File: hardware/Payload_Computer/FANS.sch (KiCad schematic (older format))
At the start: 0 parts

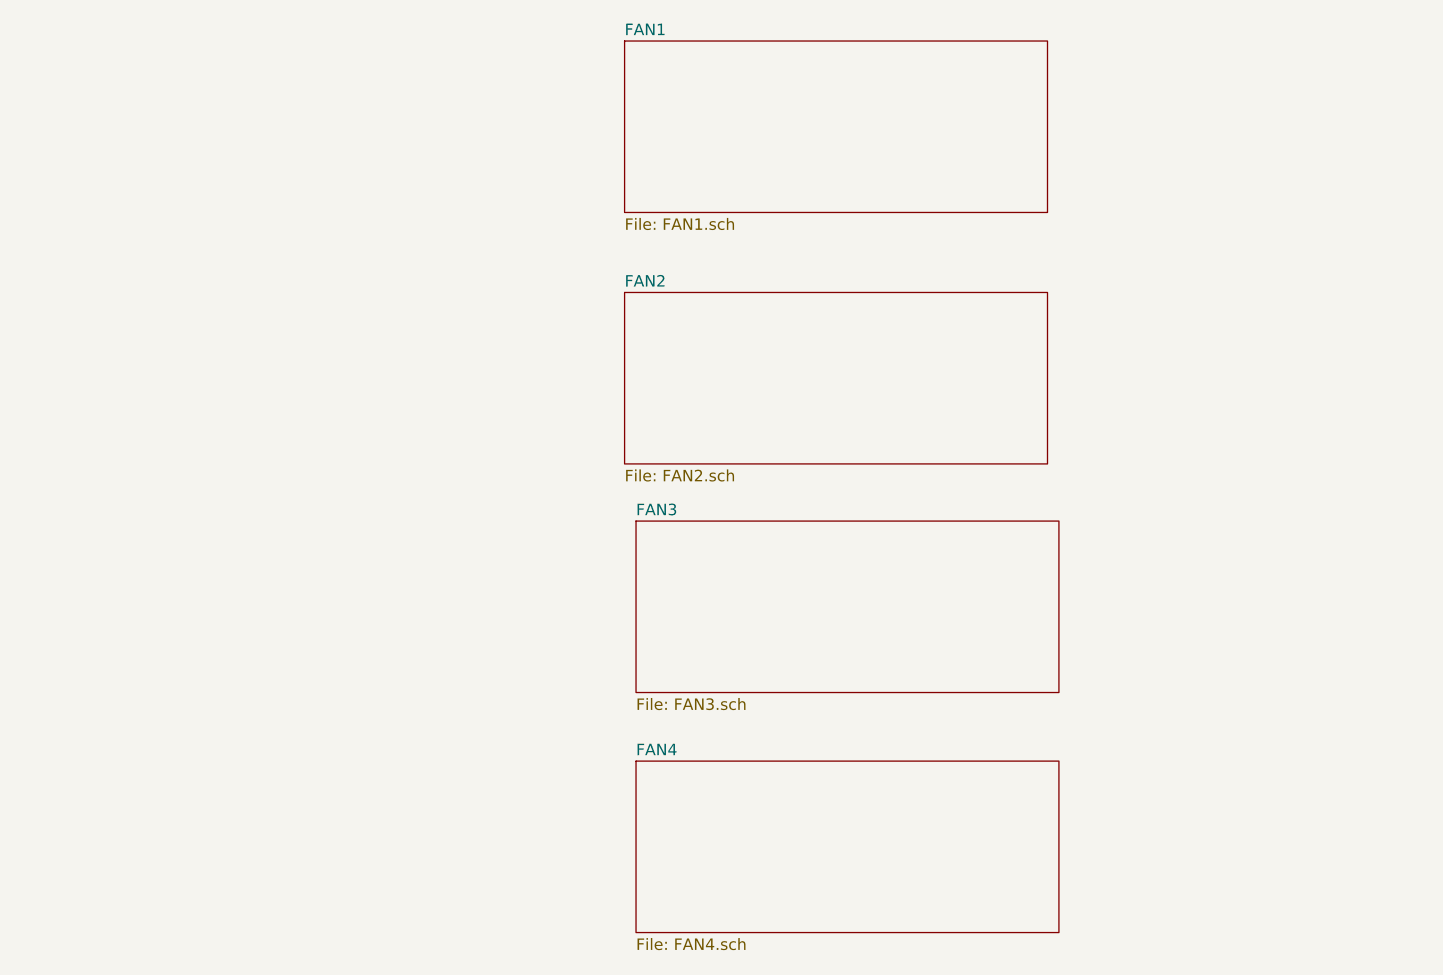
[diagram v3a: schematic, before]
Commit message: Finished Fan Schematic. Working on Servos
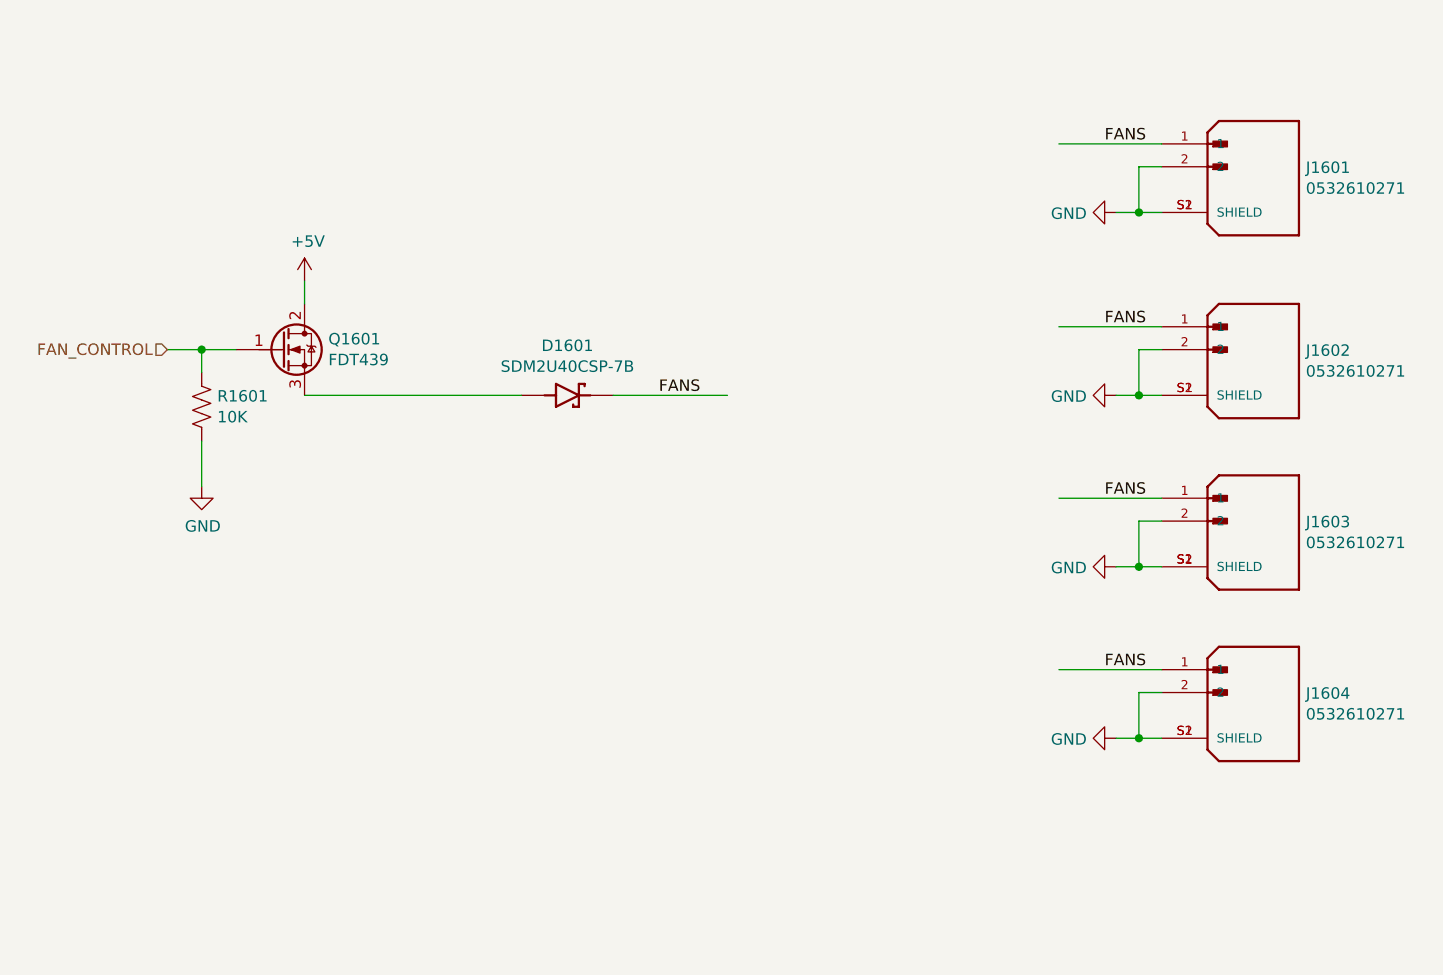
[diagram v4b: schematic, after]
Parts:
- added D1601: SDM2U40CSP-7B, SDM2U40CSP-7B:DIO_SDM2U40CSP-7B, symbol SDM2U40CSP-7B:SDM2U40CSP-7B
- added J1601, J1602, J1603, J1604: 0532610271, 0532610271:MOLEX_0532610271, symbol 0532610271:0532610271
- added Q1601: FDT439, Package_TO_SOT_SMD:SOT-223-3_TabPin2, symbol Transistor_FET:BSP129
- added R1601: 10K, Resistor_SMD:R_0603_1608Metric_Pad0.98x0.95mm_HandSolder, symbol Device:R_US
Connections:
- net labels added: +5V, FANS, FAN_CONTROL, GND
- wire segments 0 -> 27
